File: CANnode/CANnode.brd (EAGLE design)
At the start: 60.1 x 58.6 mm, 247 parts, among them IC1 ISO1050DUB, IC2 ISO1050DUB, Q1 FDV302P, Q3 FDV302P, U1 LM324PW, U10 FT2232HL, U11 93LC56C-I/SN, U2 TPS70445_PWP_24, U3 LM324PW, U4 LM324PW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

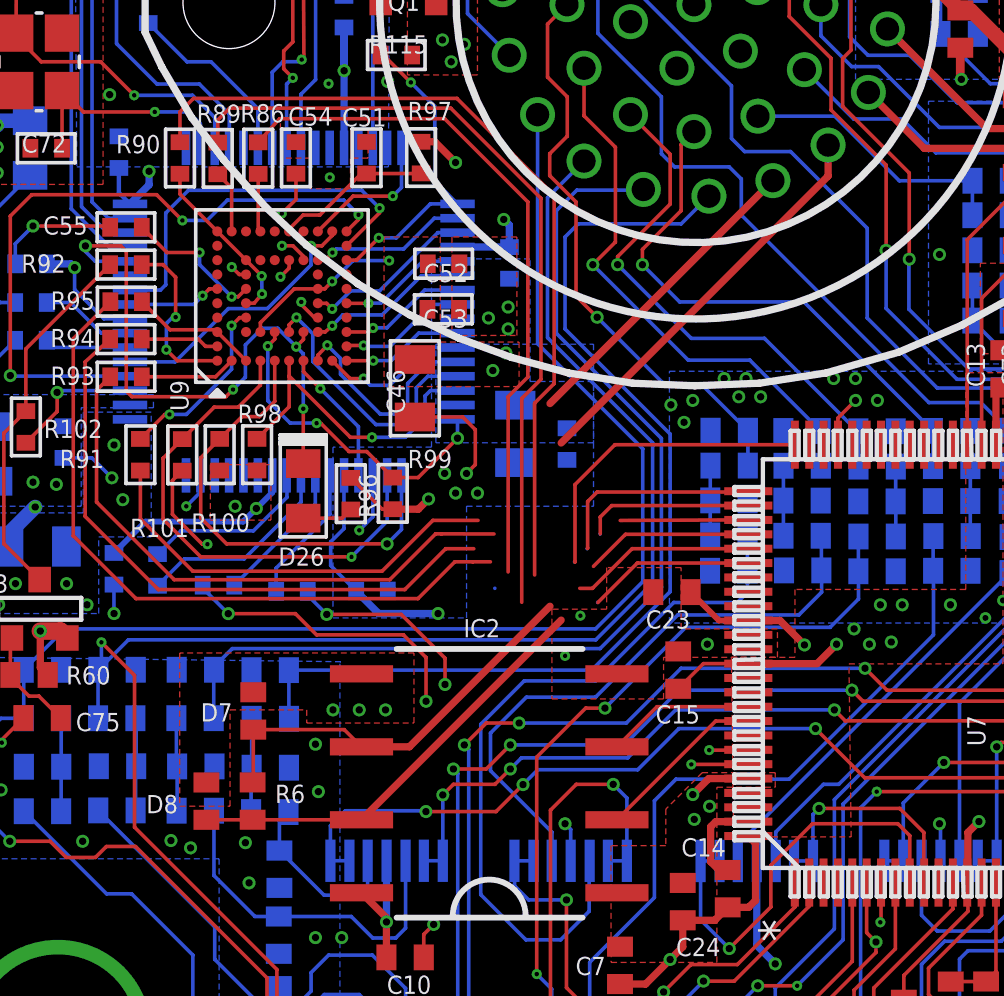
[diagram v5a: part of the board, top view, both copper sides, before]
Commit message: Routed TCK without vias
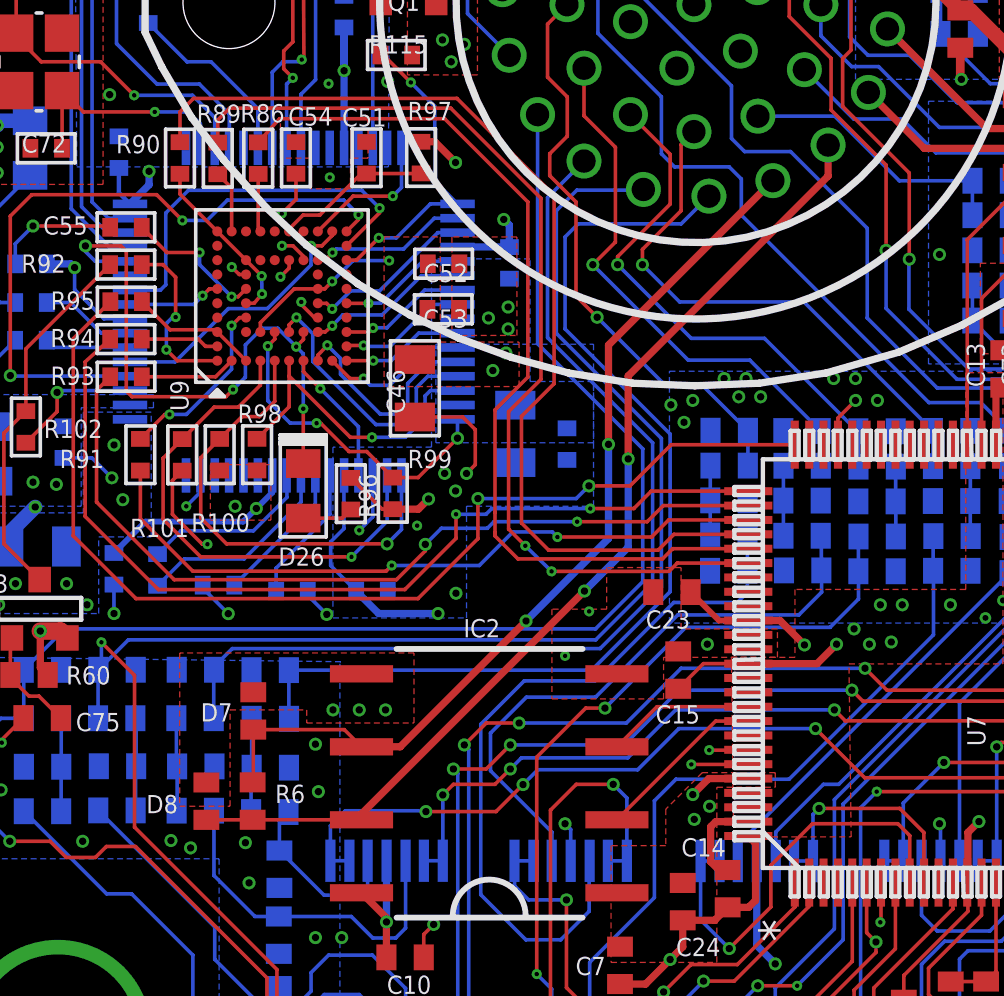
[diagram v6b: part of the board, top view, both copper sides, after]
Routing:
- net CAN2L: track 25.5 -> 32.3 mm, vias 0 -> 2
- net CAN2H: track 29.5 -> 35.6 mm, vias 0 -> 2
- net MCU_TDO: track 19.4 -> 24.5 mm, vias 0 -> 2
- net MCU_TRSTN: track 29.1 -> 32.7 mm, vias 0 -> 2
- net MCU_TDI: track 26.2 -> 29.7 mm, vias 0 -> 2
- net MCU_TMS: track 35.6 -> 37.7 mm, vias 0 -> 3
- net MCU_RTCK: track 30.5 -> 32.3 mm
- net MCU_TCK: track 35.0 -> 36.0 mm
- net SCI1_TX: track 22.5 -> 21.6 mm, vias 3 -> 2
- net MCU_RESET: track 33.7 -> 34.5 mm, vias 0 -> 2
- net SCI1_RX: track 18.3 -> 17.7 mm, vias 3 -> 2
- net GND: vias 133 -> 134

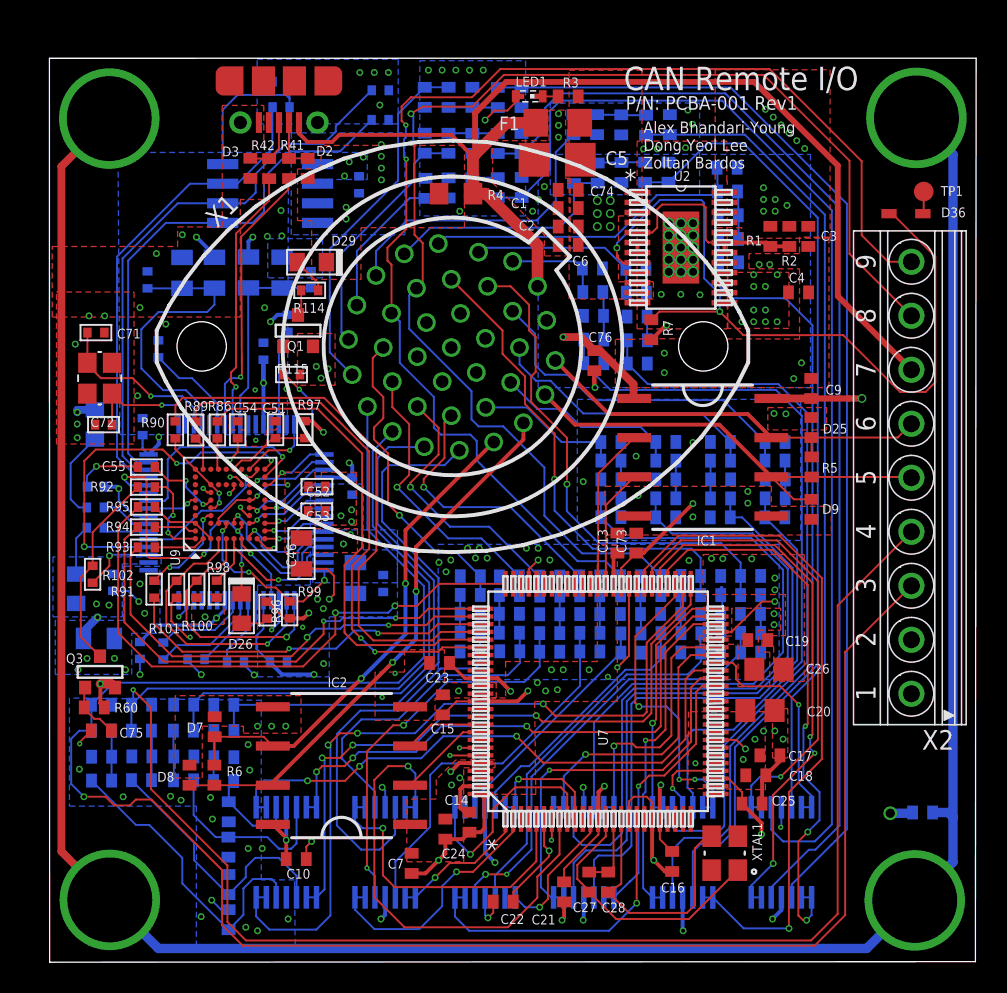
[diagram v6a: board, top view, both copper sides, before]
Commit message: Moved LEDs from bottom to top layer
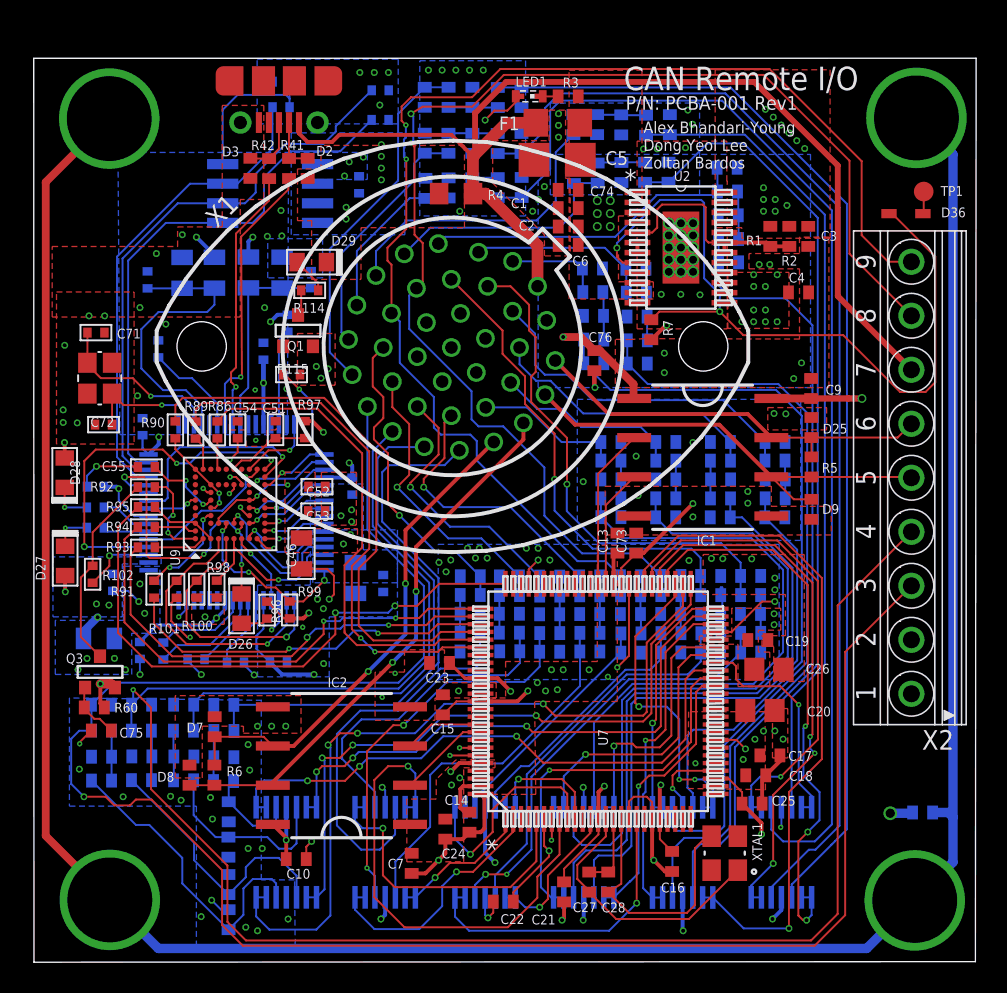
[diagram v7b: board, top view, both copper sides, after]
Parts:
- moved D28 3.58 mm to (0.82, 30.7), flipped to the top
- moved D27 2.02 mm to (0.65, 25.2), flipped to the top
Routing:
- net N$43: track 5.82 -> 2.74 mm, vias 0 -> 1
- net CGND: track 162.2 -> 163.0 mm
- net +3V3: track 84.4 -> 85.2 mm, vias 57 -> 58
- net N$42: track 3.29 -> 2.59 mm, vias 0 -> 1
- net GND: vias 134 -> 135
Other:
- board size 60.1 x 58.6 mm -> 61.1 x 58.6 mm

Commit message: Tidying silkscreen on bottom layer
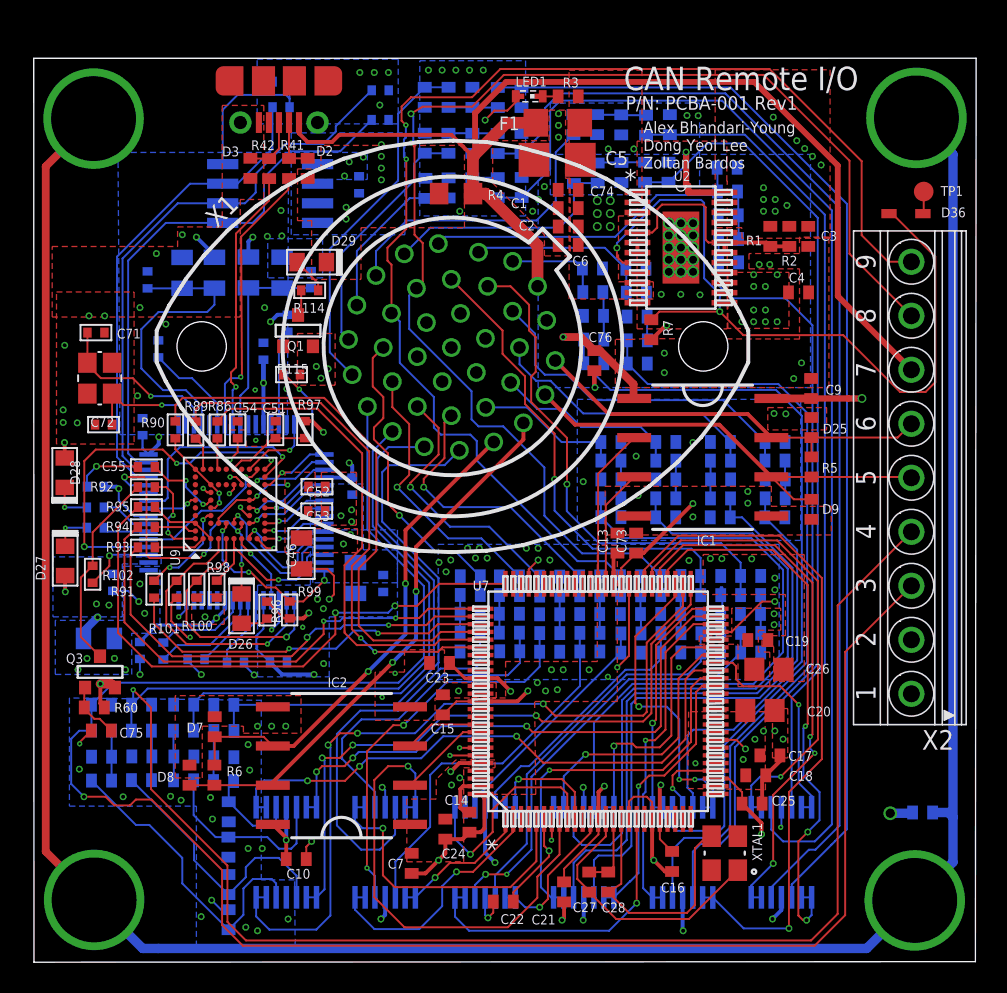
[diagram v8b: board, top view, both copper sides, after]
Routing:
- net GND: track 82.8 -> 87.9 mm, vias 135 -> 136
- net +3V3: vias 58 -> 57
